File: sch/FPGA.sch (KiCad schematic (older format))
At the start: 18 parts, among them J1 CLP-105-02-F-D, U2 iCE40-HX8K-CT256, U3 N25Q032A13EF440F, Y1 ECS-5032MV-120-BM-TR

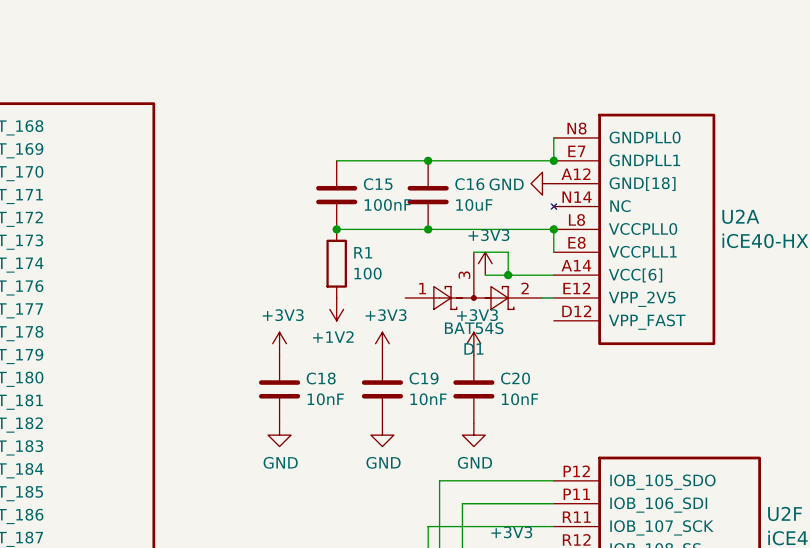
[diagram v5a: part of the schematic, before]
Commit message: VCC is 1V2 not 3V3
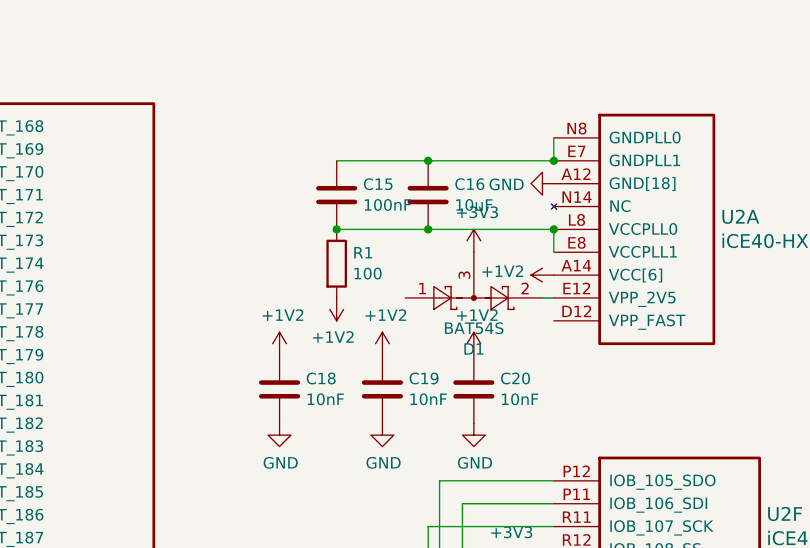
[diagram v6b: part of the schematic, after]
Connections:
- net +1V2: now also C18.1, C19.1, C20.1, U2.A14 (VCC[6]), U2.F10 (VCC[6]), U2.F6 (VCC[6]), U2.K10 (VCC[6]), U2.K6 (VCC[6]), U2.L2 (VCC[6])
- net +3V3: no longer C18.1, C19.1, C20.1, U2.A14 (VCC[6]), U2.F10 (VCC[6]), U2.F6 (VCC[6]), U2.K10 (VCC[6]), U2.K6 (VCC[6]), U2.L2 (VCC[6])
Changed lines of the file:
@@
 L power:+3V3 #PWR0163
 U 1 1 60B87561
-P 9350 1550
-F 0 "#PWR0163" H 9350 1400 50  0001 C CNN
-F 1 "+3V3" H 9365 1723 50  0000 C CNN
-F 2 "" H 9350 1550 50  0001 C CNN
-F 3 "" H 9350 1550 50  0001 C CNN
-	1    9350 1550
+P 9300 1450
+F 0 "#PWR0163" H 9300 1300 50  0001 C CNN
+F 1 "+3V3" H 9315 1623 50  0000 C CNN
+F 2 "" H 9300 1450 50  0001 C CNN
+F 3 "" H 9300 1450 50  0001 C CNN
+	1    9300 1450
 	1    0    0    -1
 $EndComp
@@
 	0    1    1    0
 $EndComp
-Wire Wire Line
-	9650 1550 9450 1550
 Wire Wire Line
 	9650 1450 9650 1350
@@
 $EndComp
 $Comp
-L power:+3V3 #PWR?
-U 1 1 60C087CD
-P 8900 1900
-AR Path="/60C087CD" Ref="#PWR?"  Part="1"
-AR Path="/60A42C75/60C087CD" Ref="#PWR03"  Part="1"
-F 0 "#PWR03" H 8900 1750 50  0001 C CNN
-F 1 "+3V3" H 8915 2073 50  0000 C CNN
-F 2 "" H 8900 1900 50  0001 C CNN
-F 3 "" H 8900 1900 50  0001 C CNN
-	1    8900 1900
-	1    0    0    -1
-$EndComp
-$Comp
 L Device:C C?
 U 1 1 60C1F86D
@@
 $EndComp
 $Comp
-L power:+3V3 #PWR?
-U 1 1 60C1F879
-P 9300 1900
-AR Path="/60C1F879" Ref="#PWR?"  Part="1"
-AR Path="/60A42C75/60C1F879" Ref="#PWR05"  Part="1"
-F 0 "#PWR05" H 9300 1750 50  0001 C CNN
-F 1 "+3V3" H 9315 2073 50  0000 C CNN
-F 2 "" H 9300 1900 50  0001 C CNN
-F 3 "" H 9300 1900 50  0001 C CNN
-	1    9300 1900
-	1    0    0    -1
-$EndComp
-$Comp
 L Device:C C?
 U 1 1 60C21622
@@
 F 3 "" H 8450 2200 50  0001 C CNN
 	1    8450 2200
-	1    0    0    -1
-$EndComp
-$Comp
-L power:+3V3 #PWR?
-U 1 1 60C2162E
-P 8450 1900
-AR Path="/60C2162E" Ref="#PWR?"  Part="1"
-AR Path="/60A42C75/60C2162E" Ref="#PWR01"  Part="1"
-F 0 "#PWR01" H 8450 1750 50  0001 C CNN
-F 1 "+3V3" H 8465 2073 50  0000 C CNN
-F 2 "" H 8450 1900 50  0001 C CNN
-F 3 "" H 8450 1900 50  0001 C CNN
-	1    8450 1900
 	1    0    0    -1
 $EndComp
@@
 $EndComp
 Wire Wire Line
-	9300 1450 9450 1450
-Wire Wire Line
-	9450 1450 9450 1550
-Connection ~ 9450 1550
-Wire Wire Line
-	9450 1550 9350 1550
-Wire Wire Line
 	9600 1650 9650 1650
+$Comp
+L power:+1V2 #PWR?
+U 1 1 608E607D
+P 9650 1550
+F 0 "#PWR?" H 9650 1400 50  0001 C CNN
+F 1 "+1V2" V 9665 1678 50  0000 L CNN
+F 2 "" H 9650 1550 50  0001 C CNN
+F 3 "" H 9650 1550 50  0001 C CNN
+	1    9650 1550
+	0    -1   -1   0
+$EndComp
+$Comp
+L power:+1V2 #PWR?
+U 1 1 6090D69B
+P 8450 1900
+F 0 "#PWR?" H 8450 1750 50  0001 C CNN
+F 1 "+1V2" H 8465 2073 50  0000 C CNN
+F 2 "" H 8450 1900 50  0001 C CNN
+F 3 "" H 8450 1900 50  0001 C CNN
+	1    8450 1900
+	1    0    0    -1
+$EndComp
+$Comp
+L power:+1V2 #PWR?
+U 1 1 6090EE4F
+P 8900 1900
+F 0 "#PWR?" H 8900 1750 50  0001 C CNN
+F 1 "+1V2" H 8915 2073 50  0000 C CNN
+F 2 "" H 8900 1900 50  0001 C CNN
+F 3 "" H 8900 1900 50  0001 C CNN
+	1    8900 1900
+	1    0    0    -1
+$EndComp
+$Comp
+L power:+1V2 #PWR?
+U 1 1 60910275
+P 9300 1900
+F 0 "#PWR?" H 9300 1750 50  0001 C CNN
+F 1 "+1V2" H 9315 2073 50  0000 C CNN
+F 2 "" H 9300 1900 50  0001 C CNN
+F 3 "" H 9300 1900 50  0001 C CNN
+	1    9300 1900
+	1    0    0    -1
+$EndComp
 $EndSCHEMATC

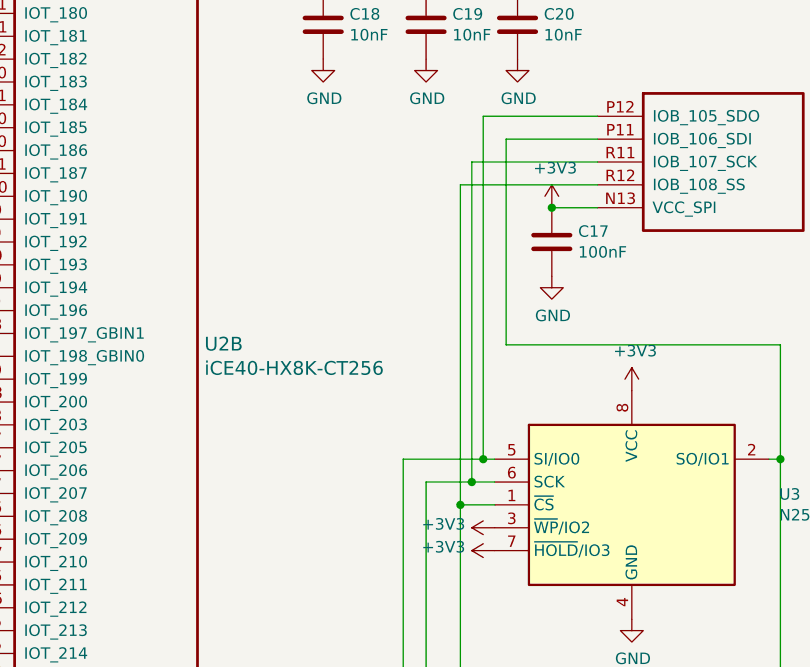
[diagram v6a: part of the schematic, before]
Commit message: Add recommended SPI pullups
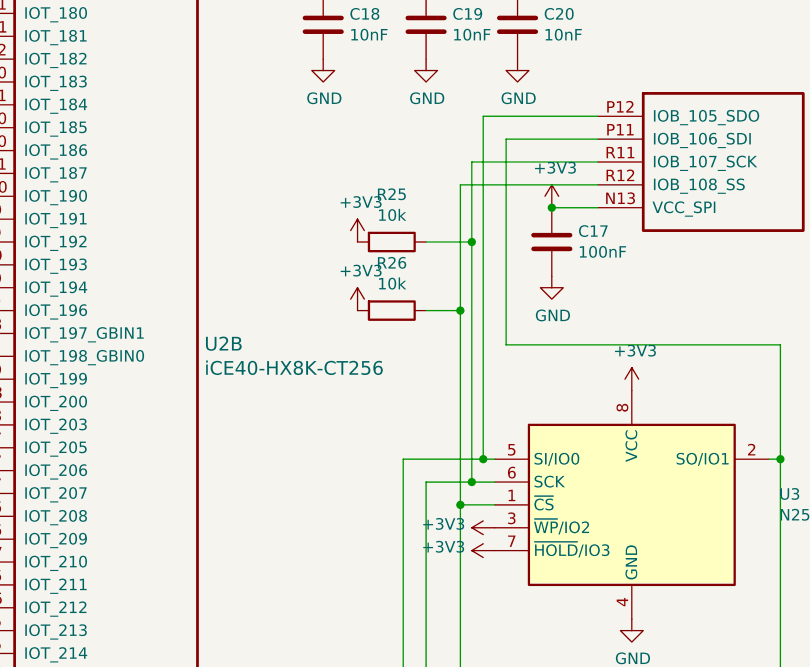
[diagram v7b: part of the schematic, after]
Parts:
- added R25, R26: 10k, Resistor_SMD:R_0402_1005Metric, symbol Device:R
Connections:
- net +3V3: now also R25.2, R26.2
- net at J1.1, U2.R11 (IOB_107_SCK), U3.6 (SCK): now also R25.1
- net at J1.7, U2.R12 (IOB_108_SS), U3.1 (~CS): now also R26.1
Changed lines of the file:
@@
 	9200 4050 9100 4050
 Wire Wire Line
-	9100 4050 9100 2650
+	9100 4050 9100 3000
 Wire Wire Line
 	9100 2650 9650 2650
@@
 	9650 2750 9050 2750
 Wire Wire Line
-	9050 2750 9050 4150
+	9050 2750 9050 3300
 Wire Wire Line
 	9050 4150 9200 4150
@@
 	9600 1650 9650 1650
 $Comp
-L power:+1V2 #PWR?
+L power:+1V2 #PWR0199
 U 1 1 608E607D
 P 9650 1550
-F 0 "#PWR?" H 9650 1400 50  0001 C CNN
+F 0 "#PWR0199" H 9650 1400 50  0001 C CNN
 F 1 "+1V2" V 9665 1678 50  0000 L CNN
 F 2 "" H 9650 1550 50  0001 C CNN
@@
 $EndComp
 $Comp
-L power:+1V2 #PWR?
+L power:+1V2 #PWR0200
 U 1 1 6090D69B
 P 8450 1900
-F 0 "#PWR?" H 8450 1750 50  0001 C CNN
+F 0 "#PWR0200" H 8450 1750 50  0001 C CNN
 F 1 "+1V2" H 8465 2073 50  0000 C CNN
 F 2 "" H 8450 1900 50  0001 C CNN
@@
 $EndComp
 $Comp
-L power:+1V2 #PWR?
+L power:+1V2 #PWR0201
 U 1 1 6090EE4F
 P 8900 1900
-F 0 "#PWR?" H 8900 1750 50  0001 C CNN
+F 0 "#PWR0201" H 8900 1750 50  0001 C CNN
 F 1 "+1V2" H 8915 2073 50  0000 C CNN
 F 2 "" H 8900 1900 50  0001 C CNN
@@
 $EndComp
 $Comp
-L power:+1V2 #PWR?
+L power:+1V2 #PWR0202
 U 1 1 60910275
 P 9300 1900
-F 0 "#PWR?" H 9300 1750 50  0001 C CNN
+F 0 "#PWR0202" H 9300 1750 50  0001 C CNN
 F 1 "+1V2" H 9315 2073 50  0000 C CNN
 F 2 "" H 9300 1900 50  0001 C CNN
@@
 	1    0    0    -1
 $EndComp
+$Comp
+L Device:R R25
+U 1 1 6096B305
+P 8750 3000
+F 0 "R25" V 8543 3000 50  0000 C CNN
+F 1 "10k" V 8634 3000 50  0000 C CNN
+F 2 "Resistor_SMD:R_0402_1005Metric" V 8680 3000 50  0001 C CNN
+F 3 "~" H 8750 3000 50  0001 C CNN
+	1    8750 3000
+	0    1    1    0
+$EndComp
+$Comp
+L Device:R R26
+U 1 1 6096CAF2
+P 8750 3300
+F 0 "R26" V 8543 3300 50  0000 C CNN
+F 1 "10k" V 8634 3300 50  0000 C CNN
+F 2 "Resistor_SMD:R_0402_1005Metric" V 8680 3300 50  0001 C CNN
+F 3 "~" H 8750 3300 50  0001 C CNN
+	1    8750 3300
+	0    1    1    0
+$EndComp
+$Comp
+L power:+3V3 #PWR01
+U 1 1 6096F032
+P 8600 3000
+F 0 "#PWR01" H 8600 2850 50  0001 C CNN
+F 1 "+3V3" H 8615 3173 50  0000 C CNN
+F 2 "" H 8600 3000 50  0001 C CNN
+F 3 "" H 8600 3000 50  0001 C CNN
+	1    8600 3000
+	1    0    0    -1
+$EndComp
+$Comp
+L power:+3V3 #PWR03
+U 1 1 60970B5B
+P 8600 3300
+F 0 "#PWR03" H 8600 3150 50  0001 C CNN
+F 1 "+3V3" H 8615 3473 50  0000 C CNN
+F 2 "" H 8600 3300 50  0001 C CNN
+F 3 "" H 8600 3300 50  0001 C CNN
+	1    8600 3300
+	1    0    0    -1
+$EndComp
+Wire Wire Line
+	8900 3300 9050 3300
+Connection ~ 9050 3300
+Wire Wire Line
+	9050 3300 9050 4150
+Wire Wire Line
+	8900 3000 9100 3000
+Connection ~ 9100 3000
+Wire Wire Line
+	9100 3000 9100 2650
 $EndSCHEMATC

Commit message: V2.0 board
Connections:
- net F_D8: now reaches U2.N5 (IOB_56)
- net F_D14: now reaches U2.N6 (IOB_52)
- net F_D12: now reaches U2.N7 (IOB_66)
- net F_CE1O: now reaches U2.P10 (IOB_86)
- net F_D10: now reaches U2.P4 (IOB_54)
- net F_D9: now reaches U2.P5 (IOB_58)
- net F_D15: now reaches U2.P6 (IOB_67)
- net F_D13: now reaches U2.P7 (IOB_77)
- net F_D11: now reaches U2.P8 (IOB_72)
- net F_CE2O: now reaches U2.P9 (IOB_83)
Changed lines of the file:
@@
 Wire Wire Line
 	9100 3000 9100 2650
+Text GLabel 3400 4250 0    50   Input ~ 0
+F_CE1O
+Text GLabel 3400 3950 0    50   Input ~ 0
+F_CE2O
+Text GLabel 3400 2850 0    50   Input ~ 0
+F_D11
+Text GLabel 3400 2350 0    50   Input ~ 0
+F_D12
+Text GLabel 3400 3350 0    50   Input ~ 0
+F_D13
+Text GLabel 3400 1150 0    50   Input ~ 0
+F_D14
+Text GLabel 3400 2450 0    50   Input ~ 0
+F_D15
+Text GLabel 3400 1550 0    50   Input ~ 0
+F_D8
+Text GLabel 3400 1750 0    50   Input ~ 0
+F_D9
+Text GLabel 3400 1350 0    50   Input ~ 0
+F_D10
 $EndSCHEMATC
